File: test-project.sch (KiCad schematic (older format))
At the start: 40 parts, among them P1 CONN_01X06, P2 CONN_01X02, U1 74HC14, U2 OP275, U3 74LS163, U4 27C512-DIP

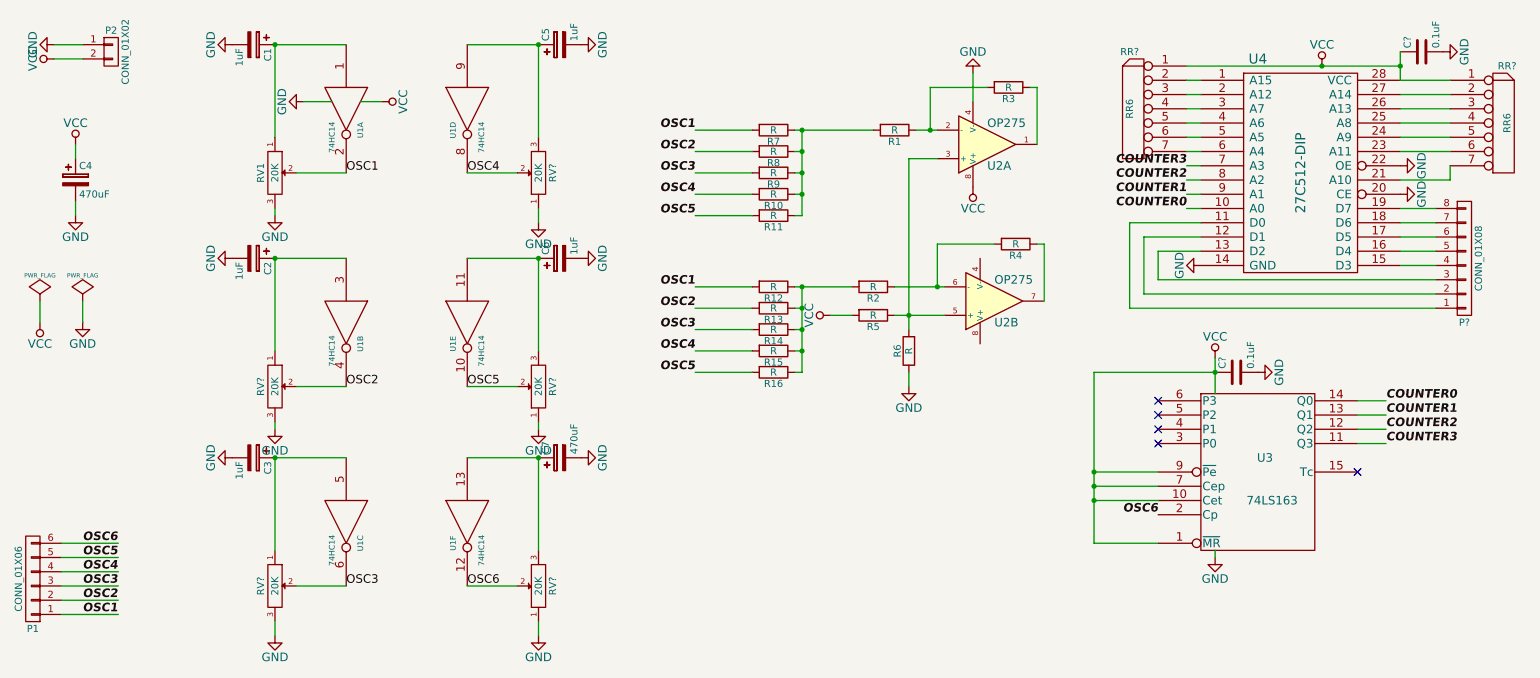
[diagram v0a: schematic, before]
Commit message: add a pair of 74LS138 chips
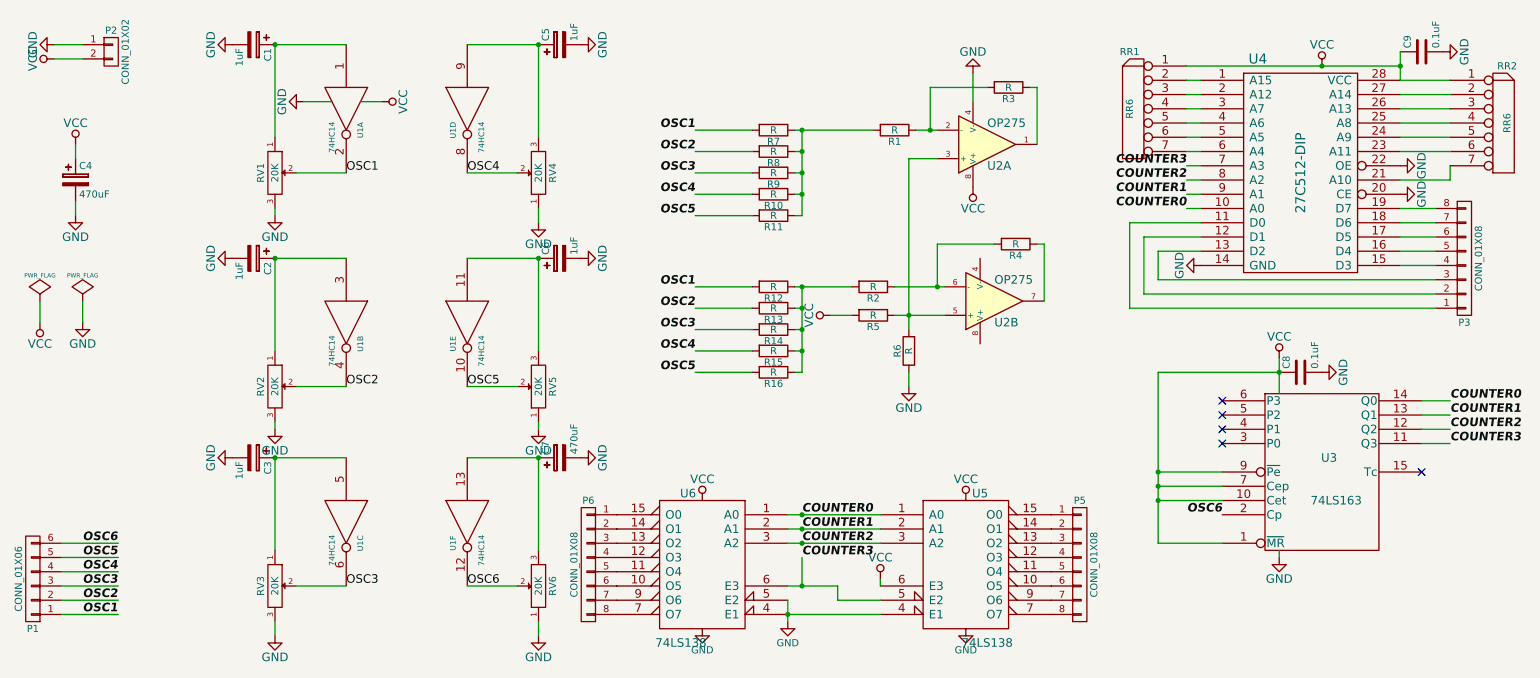
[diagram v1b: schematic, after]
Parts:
- added P5, P6: CONN_01X08, symbol CONN_01X08
- added U5, U6: 74LS138, symbol 74LS138
- gave numbers to parts that had none: 10
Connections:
- wire segments 122 -> 132
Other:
- moved on the sheet: C8, U3
